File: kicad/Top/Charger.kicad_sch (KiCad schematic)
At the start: 0 parts

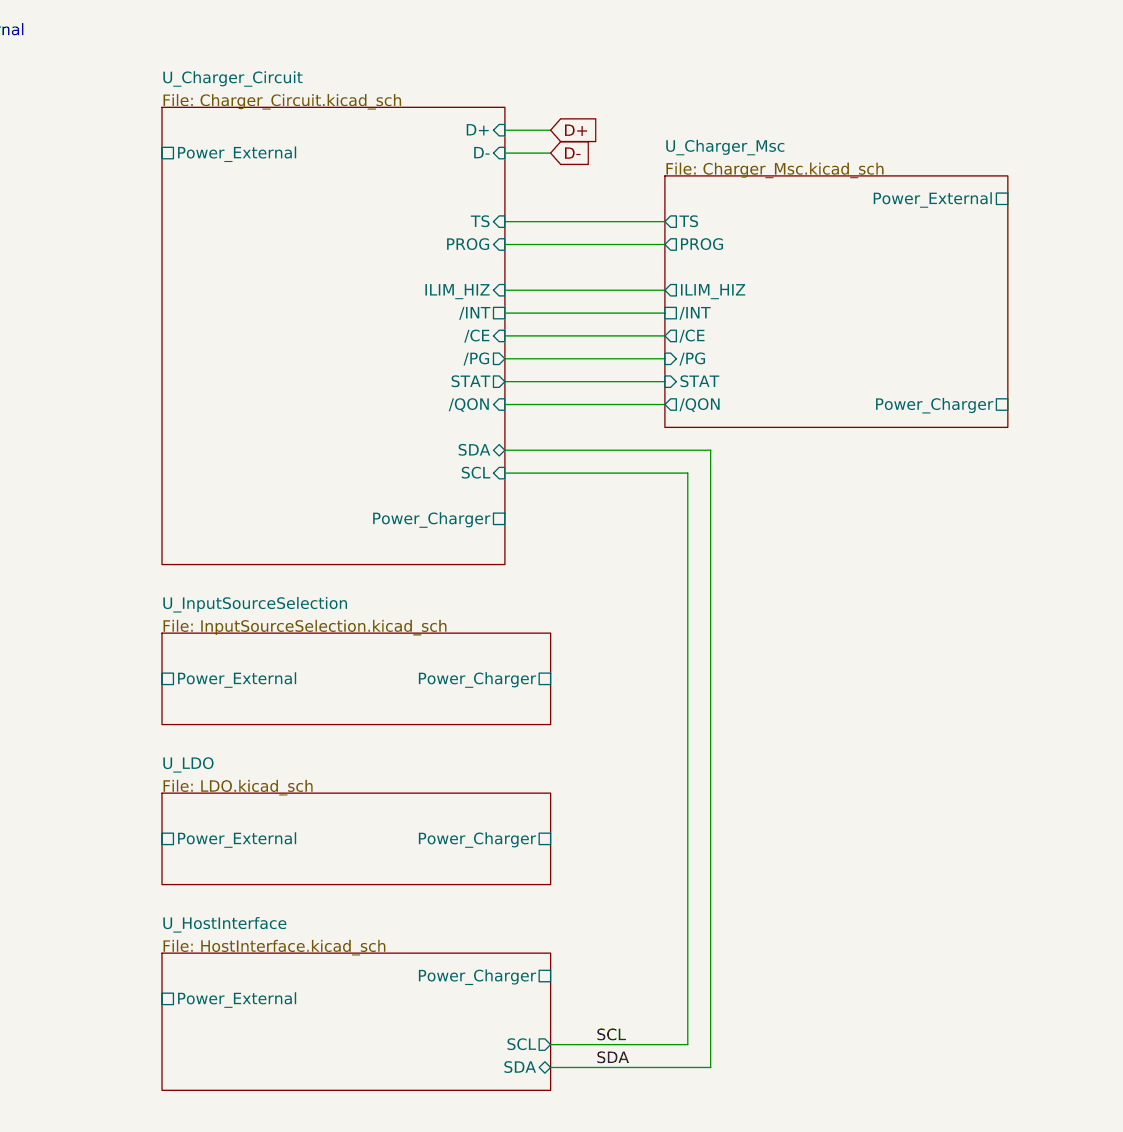
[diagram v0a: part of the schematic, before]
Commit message: Renamed sheets
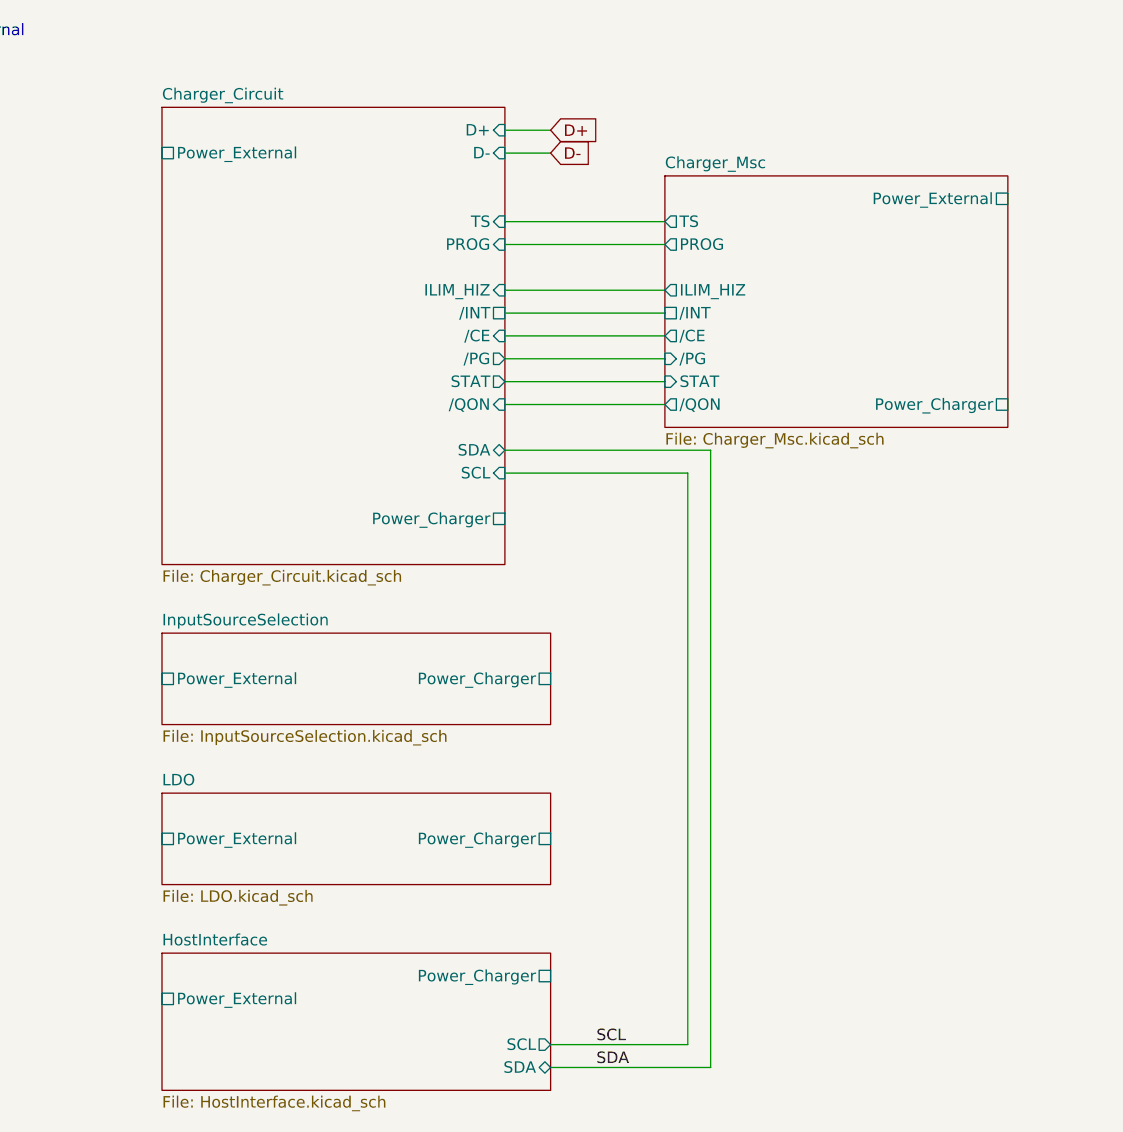
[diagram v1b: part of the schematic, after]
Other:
- sheet U_Charger_Circuit renamed Charger_Circuit
- sheet U_Charger_Msc renamed Charger_Msc
- sheet U_HostInterface renamed HostInterface
- sheet U_InputSourceSelection renamed InputSourceSelection
- sheet U_LDO renamed LDO
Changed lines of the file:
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@@
     (stroke (width 0) (type solid) (color 128 0 0 1))
     (fill (color 128 255 128 1.0000))
-    (property "Sheet name" "U_LDO" (id 0) (at 43.18 147.32 0)
+    (property "Sheet name" "LDO" (id 0) (at 43.18 149.1484 0)
       (effects (font (size 1.27 1.27)) (justify left bottom))
     )
-    (property "Sheet file" "LDO.kicad_sch" (id 1) (at 43.18 149.86 0)
-      (effects (font (size 1.27 1.27)) (justify left bottom))
+    (property "Sheet file" "LDO.kicad_sch" (id 1) (at 43.18 160.6046 0)
+      (effects (font (size 1.27 1.27)) (justify left top))
     )
     (pin "Power_External" passive (at 43.18 154.94 180)
@@
     (stroke (width 0) (type solid) (color 128 0 0 1))
     (fill (color 128 255 128 1.0000))
-    (property "Sheet name" "U_HostInterface" (id 0) (at 43.18 165.1 0)
+    (property "Sheet name" "HostInterface" (id 0) (at 43.18 166.9284 0)
       (effects (font (size 1.27 1.27)) (justify left bottom))
     )
-    (property "Sheet file" "HostInterface.kicad_sch" (id 1) (at 43.18 167.64 0)
-      (effects (font (size 1.27 1.27)) (justify left bottom))
+    (property "Sheet file" "HostInterface.kicad_sch" (id 1) (at 43.18 183.4646 0)
+      (effects (font (size 1.27 1.27)) (justify left top))
     )
     (pin "SCL" output (at 86.36 177.8 0)
@@
     (stroke (width 0) (type solid) (color 128 0 0 1))
     (fill (color 128 255 128 1.0000))
-    (property "Sheet name" "U_Charger_Circuit" (id 0) (at 43.18 71.12 0)
+    (property "Sheet name" "Charger_Circuit" (id 0) (at 43.18 72.9484 0)
       (effects (font (size 1.27 1.27)) (justify left bottom))
     )
-    (property "Sheet file" "Charger_Circuit.kicad_sch" (id 1) (at 43.18 73.66 0)
-      (effects (font (size 1.27 1.27)) (justify left bottom))
+    (property "Sheet file" "Charger_Circuit.kicad_sch" (id 1) (at 43.18 125.0446 0)
+      (effects (font (size 1.27 1.27)) (justify left top))
     )
     (pin "D+" input (at 81.28 76.2 0)
@@
     (stroke (width 0) (type solid) (color 128 0 0 1))
     (fill (color 128 255 128 1.0000))
-    (property "Sheet name" "U_Charger_Msc" (id 0) (at 99.06 78.74 0)
+    (property "Sheet name" "Charger_Msc" (id 0) (at 99.06 80.5684 0)
       (effects (font (size 1.27 1.27)) (justify left bottom))
     )
-    (property "Sheet file" "Charger_Msc.kicad_sch" (id 1) (at 99.06 81.28 0)
-      (effects (font (size 1.27 1.27)) (justify left bottom))
+    (property "Sheet file" "Charger_Msc.kicad_sch" (id 1) (at 99.06 109.8046 0)
+      (effects (font (size 1.27 1.27)) (justify left top))
     )
     (pin "/INT" passive (at 99.06 96.52 180)
@@
     (stroke (width 0) (type solid) (color 128 0 0 1))
     (fill (color 128 255 128 1.0000))
-    (property "Sheet name" "U_InputSourceSelection" (id 0) (at 43.18 129.54 0)
+    (property "Sheet name" "InputSourceSelection" (id 0) (at 43.18 131.3684 0)
       (effects (font (size 1.27 1.27)) (justify left bottom))
     )
-    (property "Sheet file" "InputSourceSelection.kicad_sch" (id 1) (at 43.18 132.08 0)
-      (effects (font (size 1.27 1.27)) (justify left bottom))
+    (property "Sheet file" "InputSourceSelection.kicad_sch" (id 1) (at 43.18 142.8246 0)
+      (effects (font (size 1.27 1.27)) (justify left top))
     )
     (pin "Power_External" passive (at 43.18 137.16 180)

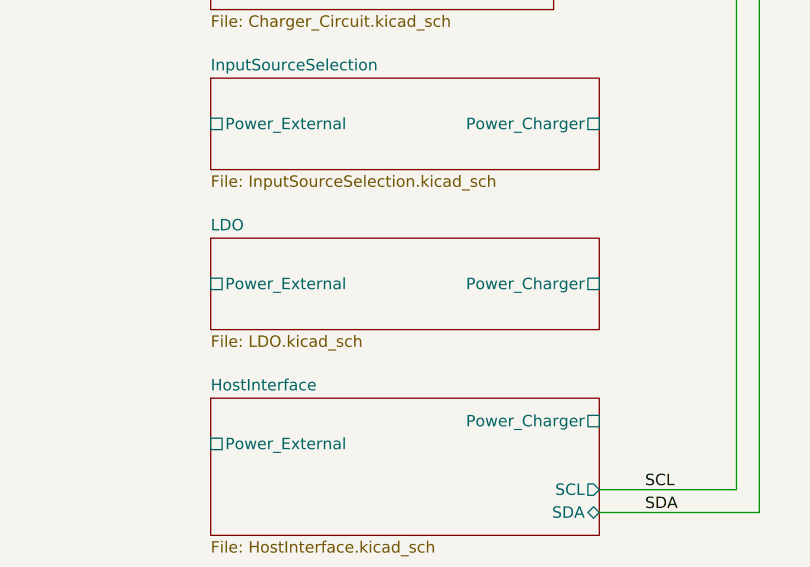
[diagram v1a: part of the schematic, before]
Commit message: Merged LDOs and moved to top sheet
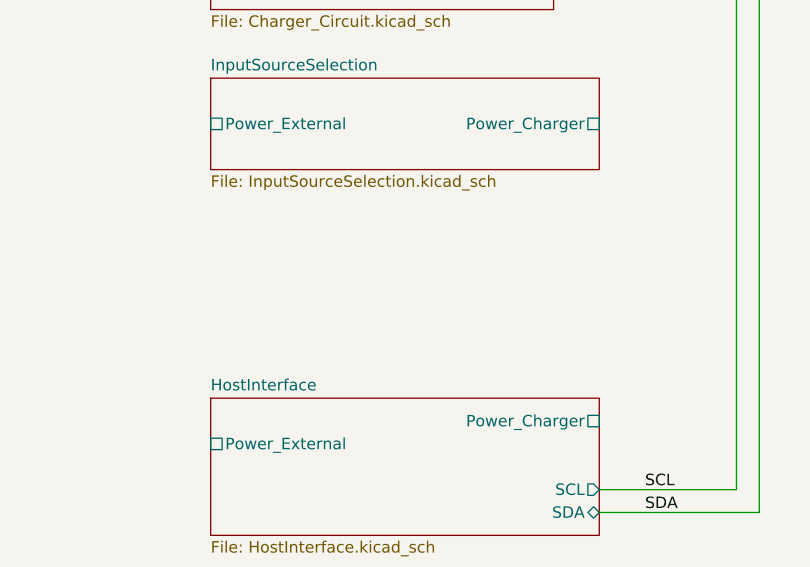
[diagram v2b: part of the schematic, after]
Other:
- removed sheet LDO
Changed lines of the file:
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@@
-    )
-  )
-  (sheet (at 43.18 149.86) (size 43.18 10.16) (fields_autoplaced)
-    (stroke (width 0) (type solid) (color 128 0 0 1))
-    (fill (color 128 255 128 1.0000))
-    (property "Sheet name" "LDO" (id 0) (at 43.18 149.1484 0)
-      (effects (font (size 1.27 1.27)) (justify left bottom))
-    )
-    (property "Sheet file" "LDO.kicad_sch" (id 1) (at 43.18 160.6046 0)
-      (effects (font (size 1.27 1.27)) (justify left top))
-    )
-    (pin "Power_External" passive (at 43.18 154.94 180)
-      (effects (font (size 1.27 1.27)) (justify left))
-    )
-    (pin "Power_Charger" passive (at 86.36 154.94 0)
-      (effects (font (size 1.27 1.27)) (justify right))
     )
   )

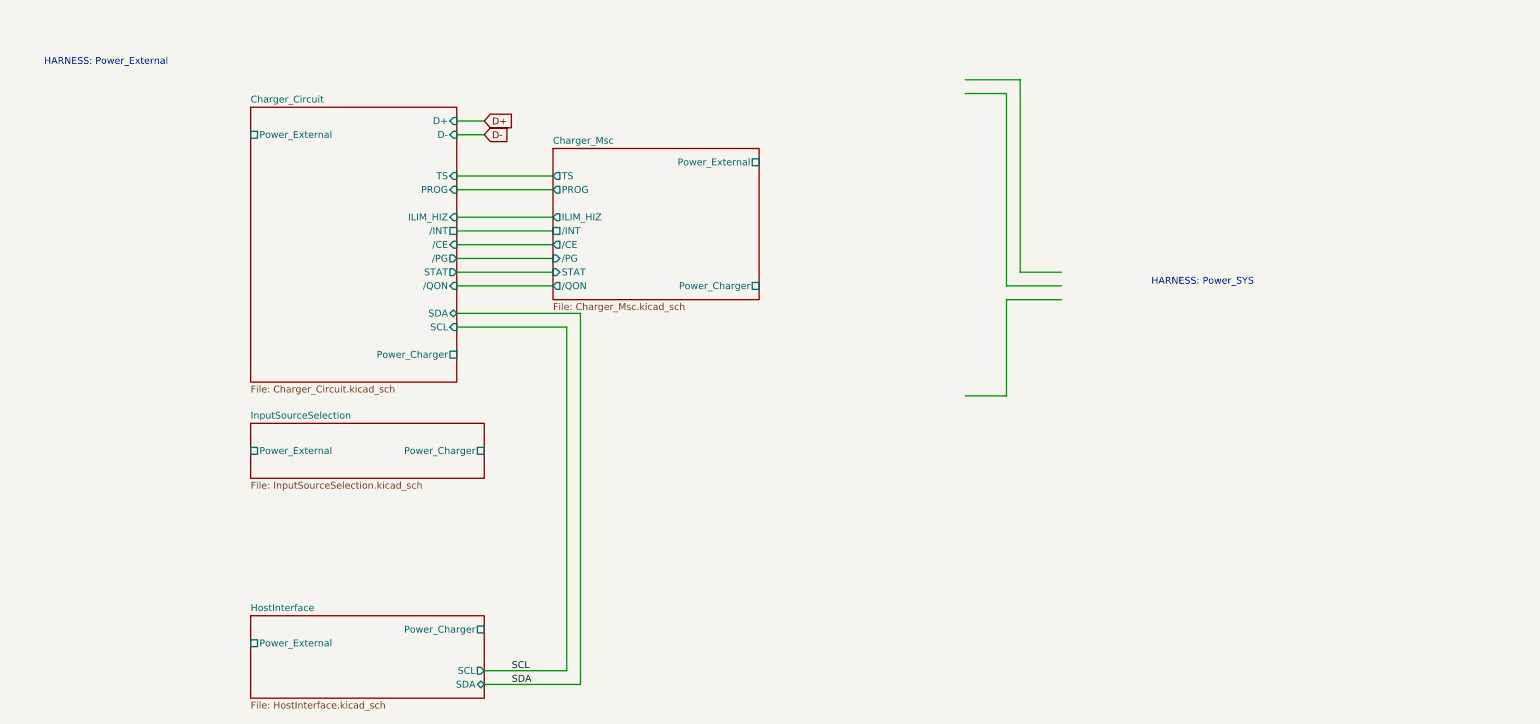
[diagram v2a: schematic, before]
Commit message: Cleaned charger sheet of floating wires
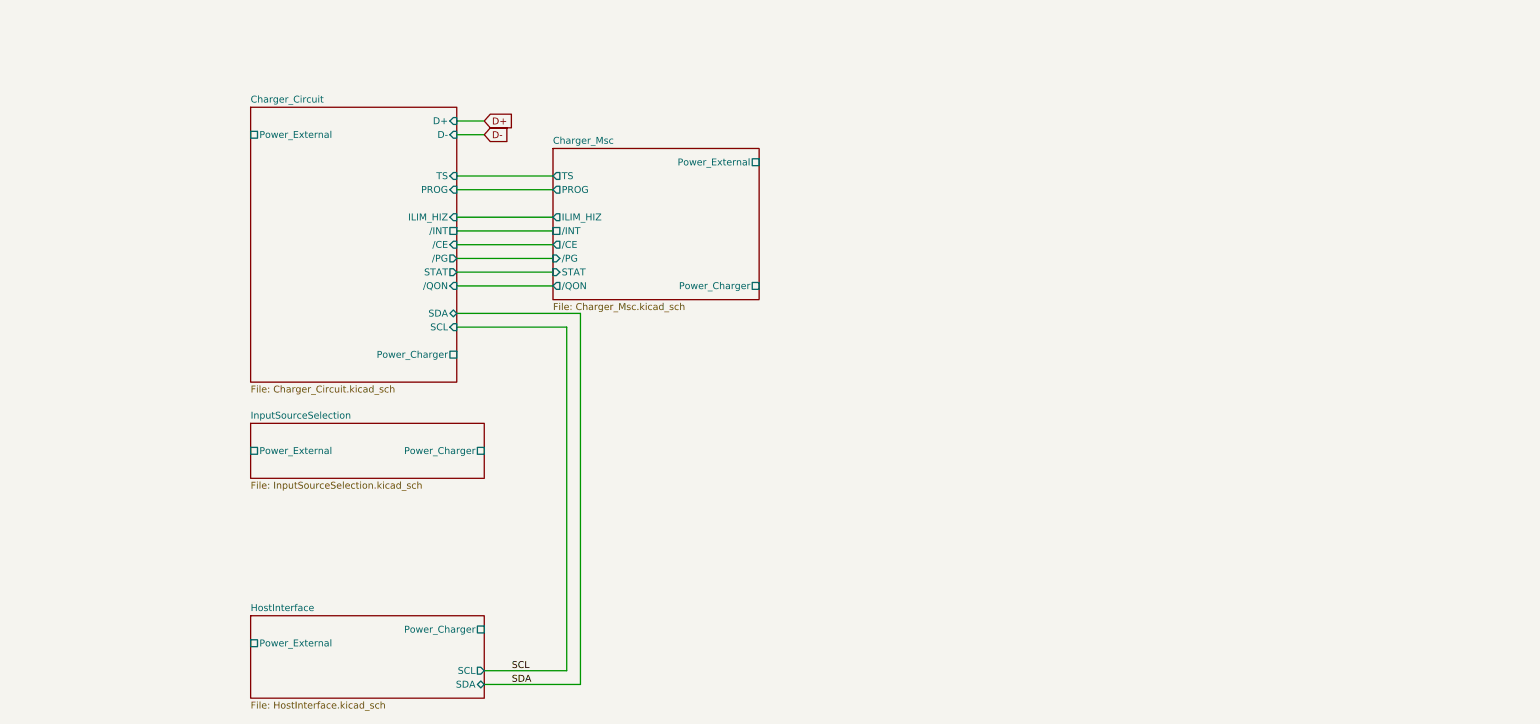
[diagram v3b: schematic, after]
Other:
- note removed: "HARNESS: Power_External"
- note removed: "HARNESS: Power_SYS"
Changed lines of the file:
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@@
-    (stroke (width 0.254) (type default) (color 0 0 0 0))
-  )
-  (wire (pts (xy 175.26 68.58) (xy 185.42 68.58))
     (stroke (width 0.254) (type default) (color 0 0 0 0))
   )
   (wire (pts (xy 86.36 177.8) (xy 101.6 177.8))
-    (stroke (width 0.254) (type default) (color 0 0 0 0))
-  )
-  (wire (pts (xy 175.26 127) (xy 182.88 127))
-    (stroke (width 0.254) (type default) (color 0 0 0 0))
-  )
-  (wire (pts (xy 182.88 127) (xy 182.88 109.22))
-    (stroke (width 0.254) (type default) (color 0 0 0 0))
-  )
-  (wire (pts (xy 182.88 71.12) (xy 182.88 106.68))
     (stroke (width 0.254) (type default) (color 0 0 0 0))
   )
@@
     (stroke (width 0.254) (type default) (color 0 0 0 0))
   )
-  (wire (pts (xy 182.88 109.22) (xy 193.04 109.22))
-    (stroke (width 0.254) (type default) (color 0 0 0 0))
-  )
   (wire (pts (xy 86.36 78.74) (xy 81.28 78.74))
     (stroke (width 0.254) (type default) (color 0 0 0 0))
   )
   (wire (pts (xy 101.6 114.3) (xy 81.28 114.3))
-    (stroke (width 0.254) (type default) (color 0 0 0 0))
-  )
-  (wire (pts (xy 185.42 68.58) (xy 185.42 104.14))
-    (stroke (width 0.254) (type default) (color 0 0 0 0))
-  )
-  (wire (pts (xy 175.26 71.12) (xy 182.88 71.12))
-    (stroke (width 0.254) (type default) (color 0 0 0 0))
-  )
-  (wire (pts (xy 185.42 104.14) (xy 193.04 104.14))
     (stroke (width 0.254) (type default) (color 0 0 0 0))
   )
@@
     (stroke (width 0.254) (type default) (color 0 0 0 0))
   )
-  (wire (pts (xy 182.88 106.68) (xy 193.04 106.68))
-    (stroke (width 0.254) (type default) (color 0 0 0 0))
-  )
-  (text "HARNESS: Power_SYS" (at 228.6 106.68 180)
-    (effects (font (size 1.27 1.27)) (justify right bottom))
-  )
-  (text "HARNESS: Power_External" (at 27.94 66.04 180)
-    (effects (font (size 1.27 1.27)) (justify right bottom))
-  )
   (label "SDA" (at 91.44 180.34 0)
